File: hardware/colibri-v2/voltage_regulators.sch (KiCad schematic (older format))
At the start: 28 parts

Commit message: Annotated Components
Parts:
- gave numbers to parts that had none: 28

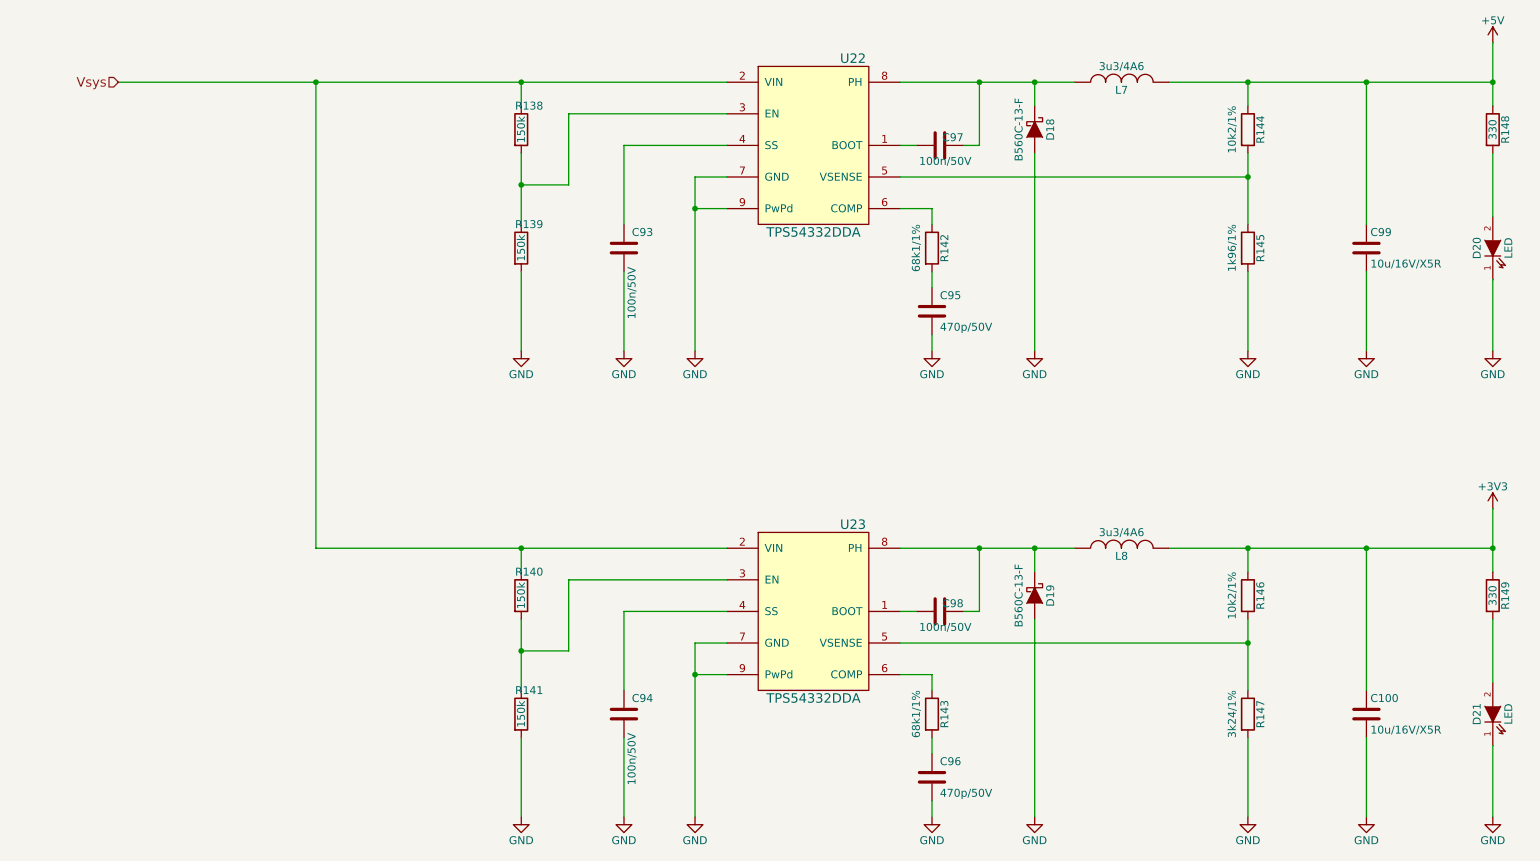
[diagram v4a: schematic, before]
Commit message: Replaced PWM buffers with SN74LVC162244A, which doesn't require pull-ups
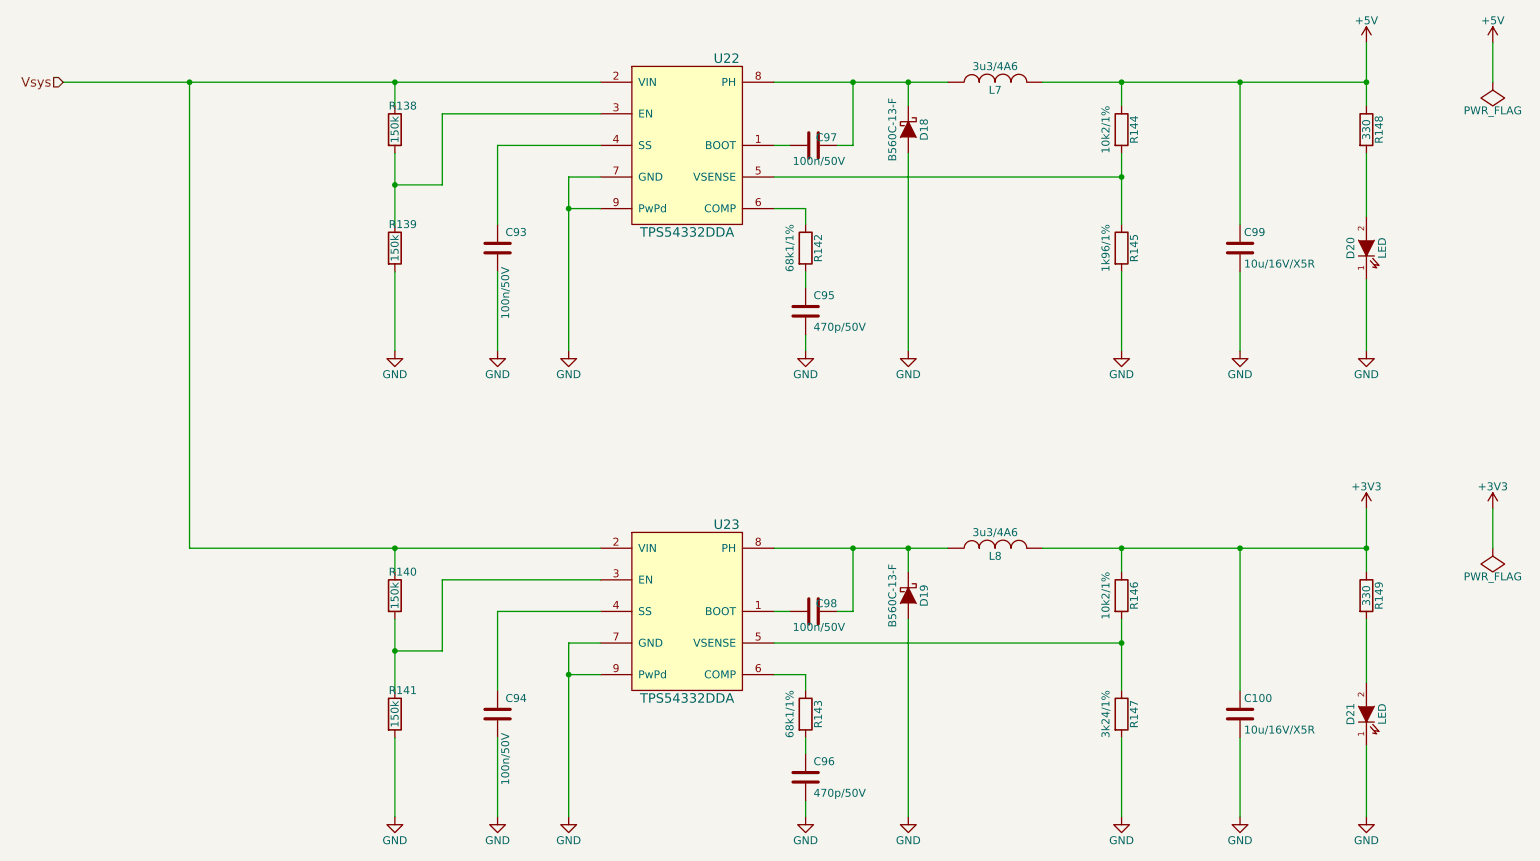
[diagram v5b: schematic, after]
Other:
- moved on the sheet: C100, C93, C94, C95, C96, C97, C98, C99, D18, D19, D20, D21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

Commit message: Re-annotated schematic
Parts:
- renumbered C93 to C89, C94 to C90, C95 to C91, C96 to C92, C97 to C93, C98 to C94, C99 to C95, C100 to C96, R138 to R141, R139 to R142, R140 to R143, R141 to R144, R142 to R145, R143 to R146, R144 to R147, R145 to R148, R146 to R149, R147 to R150, R148 to R151, R149 to R152, U22 to U20, U23 to U21

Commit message: Associated footprints for R and some of the C
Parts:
- R141, R142, R143, R144, R145, R146, R147, R148, R149, R150, R151, R152: footprint (none) -> Resistors_SMD:R_0603

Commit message: Work on cortex USB connection.
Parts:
- renumbered C95 to C?, C93 to C?, C91 to C?, C89 to C?, C96 to C?, C94 to C?, C92 to C?, C90 to C?, D20 to D?, D18 to D?, D21 to D?, D19 to D?, L7 to L?, L8 to L?, R151 to R?, R147 to R?, R148 to R?, R145 to R?, R141 to R?, R142 to R?, R152 to R?, R149 to R?, R150 to R?, R146 to R?, R143 to R?, R144 to R?, U20 to U?, U21 to U?
